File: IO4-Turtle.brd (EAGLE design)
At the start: 106.7 x 104.1 mm, 30 parts, among them CON2 RJ12/6, IC1 TC4428A, IC2 NE555S, Q1 PMBT2222, X1 0.156 Molex, X2 MSTBA5

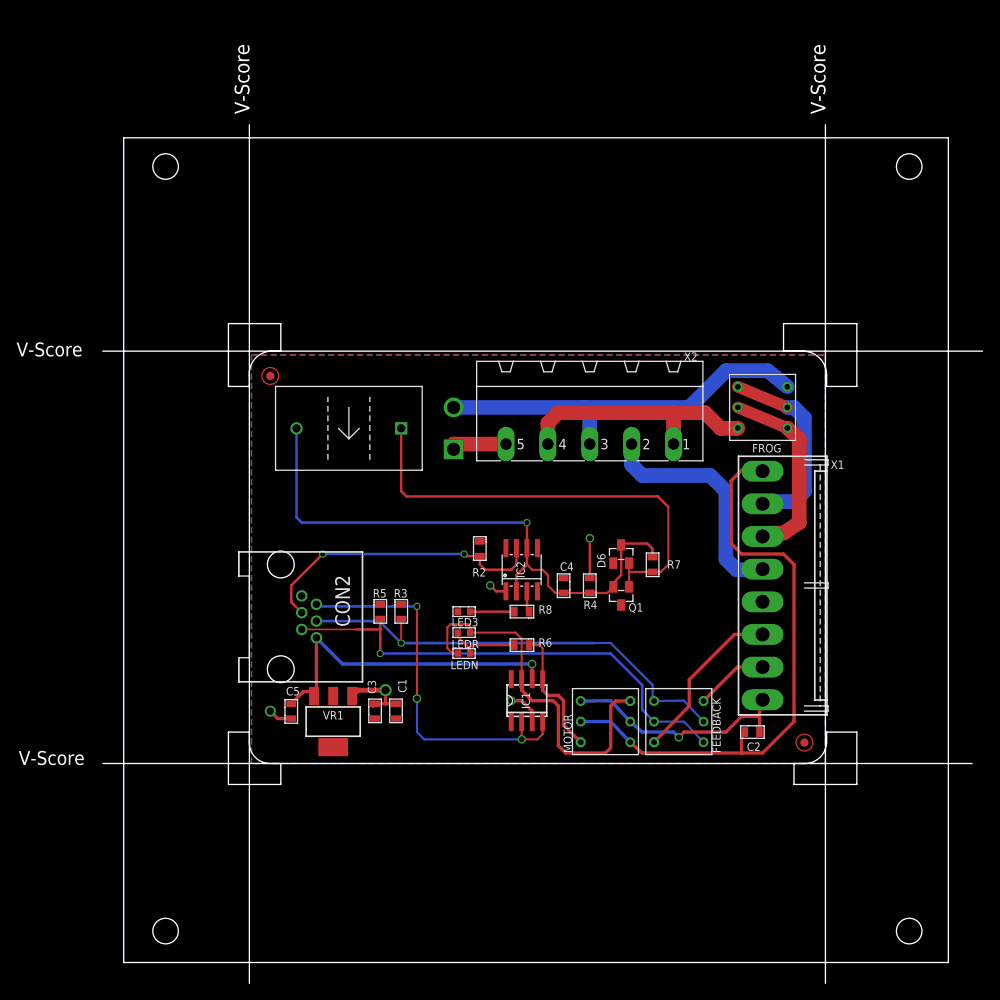
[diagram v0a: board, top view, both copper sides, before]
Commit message: cleanup, replaced LM1117 output cap
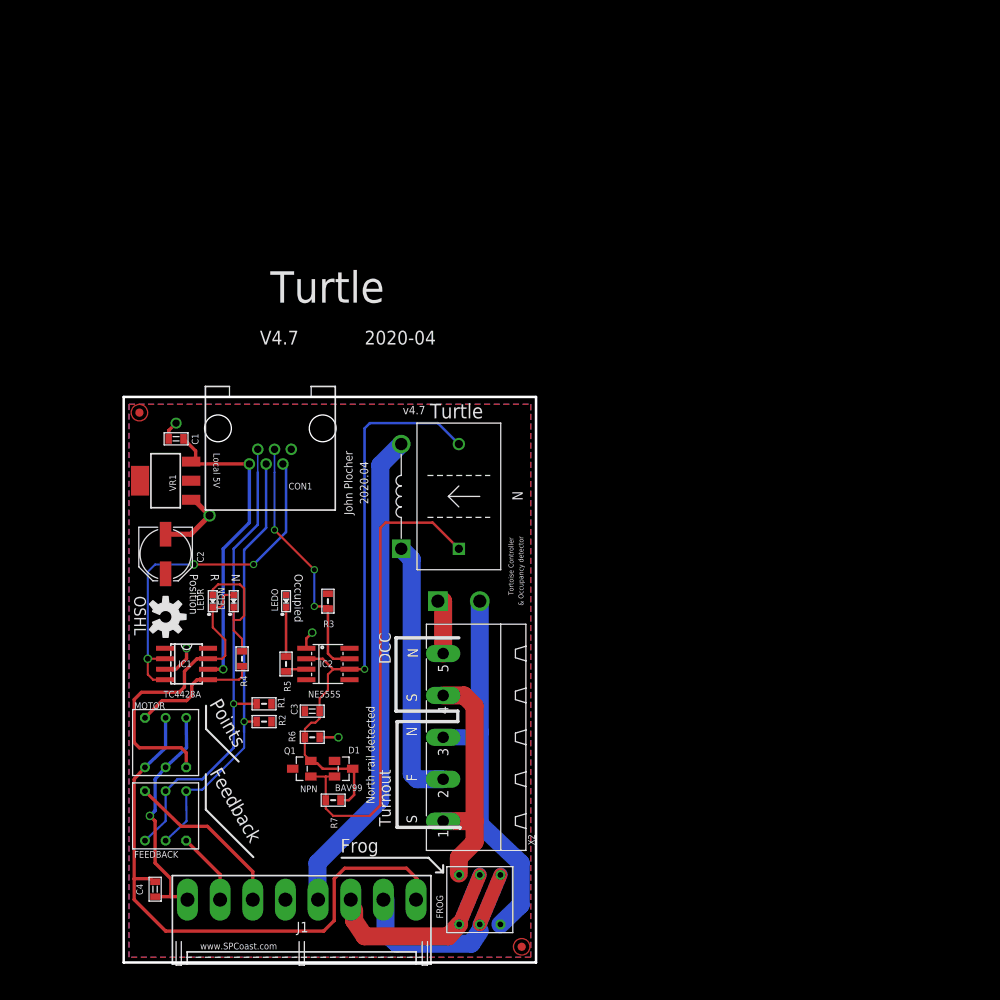
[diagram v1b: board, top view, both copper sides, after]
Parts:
- removed BOARD: BOARD70X50-HOHOLES, SPCoast:BOARD-7X5-TEMPLATE
- removed C5: 10uf, SPCoast:0805-CAP
- removed CON2: RJ12/6, SPCoast:RJ25-INVERTED
- removed D6: BAV99, SPCoast:SOT23
- removed LED3: Y, SPCoast:0603-LED
- removed R8: 1K0, SPCoast:0805-RES
- removed X1: 0.156 Molex, SPCoast:KK-156-8-F
- added CON1: RJ12/6, SPCoast:RJ25-INVERTED
- added D1: BAV99, SPCoast:SOT23
- added J1: (no value), SPCoast:KK-156-8-F
- added LEDO: Y, SPCoast:0603-LED
- added LMP1: (no value), SPCoast:BULB-3156
- added OSHW1: DOC-OSHW-LOGO-M, SPCoast:OSHW-LOGO-M
- added R1: 10k, SPCoast:0805-RES
- C2: value 0.1uf -> 100uf; device SPCoast:0805-CAP -> SPCoast:PANASONIC_D
- C3: value 10uf -> 2.2uf
- C4: value 2.2uf -> 0.1uf
- IC1: device tc442xa:SO-08 -> SPCoast:SO-08
- Q1: value PMBT2222 -> NPN
- R4: value 1M0 -> 2K0
- R5: value 10k -> 1K0
- R6: value 2K0 -> 1M0
- moved C2 74.3 mm to (5.08, 49.5), turned to 270 degrees
- moved FROG 68.8 mm to (43.2, 7.62), turned to 90 degrees
- moved FEEDBACK 63.3 mm to (5.08, 17.8), turned to 270 degrees
- moved C4 61.7 mm to (3.81, 8.89)
- moved MOTOR 53.4 mm to (5.08, 26.7), turned to 270 degrees
- moved R7 48.1 mm to (25.4, 19.7), turned to 180 degrees
- moved Q1 44.0 mm to (21.6, 23.5), turned to 90 degrees
- moved R4 43.1 mm to (14.4, 36.8)
- moved X2 42.6 mm to (43.8, 27.3), turned to 90 degrees
- moved C1 42.4 mm to (6.35, 63.5), turned to 180 degrees
- moved FID2 42.3 mm to (48.3, 1.91), turned to 270 degrees
- moved IC1 41.5 mm to (7.62, 36.2), turned to 270 degrees
- moved VR1 35.6 mm to (5.08, 58.4), turned to 90 degrees
- moved R2 33.5 mm to (17.0, 29.2), turned to 0 degrees
- moved LEDR 30.7 mm to (10.8, 43.8), turned to 270 degrees
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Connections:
- new net PROTECTED_FROG: J1.4, LMP1.P$2
- net !INORMAL: now also CON1.3, R2.1; no longer CON2.3, R3.1
- net !IOCCUPIED: now also CON1.4, R3.1; no longer CON2.4, R2.1
- net !IREVERSE: now also CON1.2, R1.1; no longer CON2.2, R5.1
- net !KNORMAL: now also CON1.5; no longer CON2.5
- net +12V: now also C1.1, CON1.1; no longer C5.1, CON2.1
- net FROG: now also LMP1.P$1; no longer X1.4
- net GND: now also C2.-, CON1.6, J1.5, R6.1; no longer C3.2, C5.2, CON2.6, R4.1, X1.5
- net M+: now also C4.1, J1.1; no longer C2.1, X1.1
- net M-: now also C4.2, J1.8; no longer C2.2, X1.8
- net N: now also J1.2; no longer X1.2
- net N$16: now also J1.6; no longer X1.6
- net N$17: now also J1.7; no longer X1.7
- net N$19: now also R4.2; no longer R6.2
- net N$2: now also D1.2; no longer D6.2
- net N$3: now also R4.1; no longer R6.1
- net N$8: now also LEDO.C, R5.1; no longer LED3.C, R8.1
- net N$9: now also R5.2; no longer R8.2
- net S: now also J1.3; no longer X1.3
- net TRIGGER: now also C3.2, D1.3, R6.2; no longer C4.2, D6.3, R4.2
- net V+: now also C2.+, LEDO.A, R1.2; no longer C1.1, C4.1, LED3.A, R5.2
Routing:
- net PROTECTED_FROG: track 0.00 -> 59.5 mm
- net N: track 23.9 -> 30.9 mm
- net N$1: track 45.4 -> 38.4 mm
- net N$3: track 8.77 -> 15.5 mm
- net S: track 23.5 -> 30.2 mm
- net !IOCCUPIED: track 36.3 -> 31.3 mm, vias 2 -> 3
- net FROG: track 28.6 -> 31.9 mm
- net N$2: track 55.8 -> 59.0 mm
- net !KNORMAL: track 46.9 -> 44.1 mm
- net GND: track 23.3 -> 20.4 mm
- net !INORMAL: track 56.0 -> 53.3 mm
- net TRIGGER: track 71.5 -> 73.3 mm
- net !IREVERSE: track 59.2 -> 57.7 mm
- net +12V: track 40.0 -> 38.7 mm
- net DCC-S: track 30.7 -> 29.4 mm
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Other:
- board size 106.7 x 104.1 mm -> 50 x 68.6 mm
- board text added: "2020-04"
- board text added: "2020.04"
- board text added: "C1"
- board text added: "C2"
- board text added: "C3"
- board text added: "C4"
- board text added: "CON1"
- board text added: "D1"
- board text added: "FEEDBACK"
- board text added: "FROG"
- board text added: "IC1"
- board text added: "IC2"
- board text added: "J1"
- board text added: "LEDN"
- board text added: "LEDO"
- board text added: "LEDR"
- board text added: "MOTOR"
- board text added: "NE555S"
- board text added: "OSHL"
- board text added: "Q1"
- board text added: "R1"
- board text added: "R2"
- board text added: "R3"
- board text added: "R4"
- board text added: "R5"
- board text added: "R6"
- board text added: "R7"
- board text added: "V4.7"
- board text added: "VR1"
- board text added: "X2"
- board text added: "v4.7"
- board text removed: "+"
- board text removed: "2018-03"
- board text removed: "2018.03"
- board text removed: "NE555"
- board text removed: "V4.6B"
- board text removed: "v4.6B"

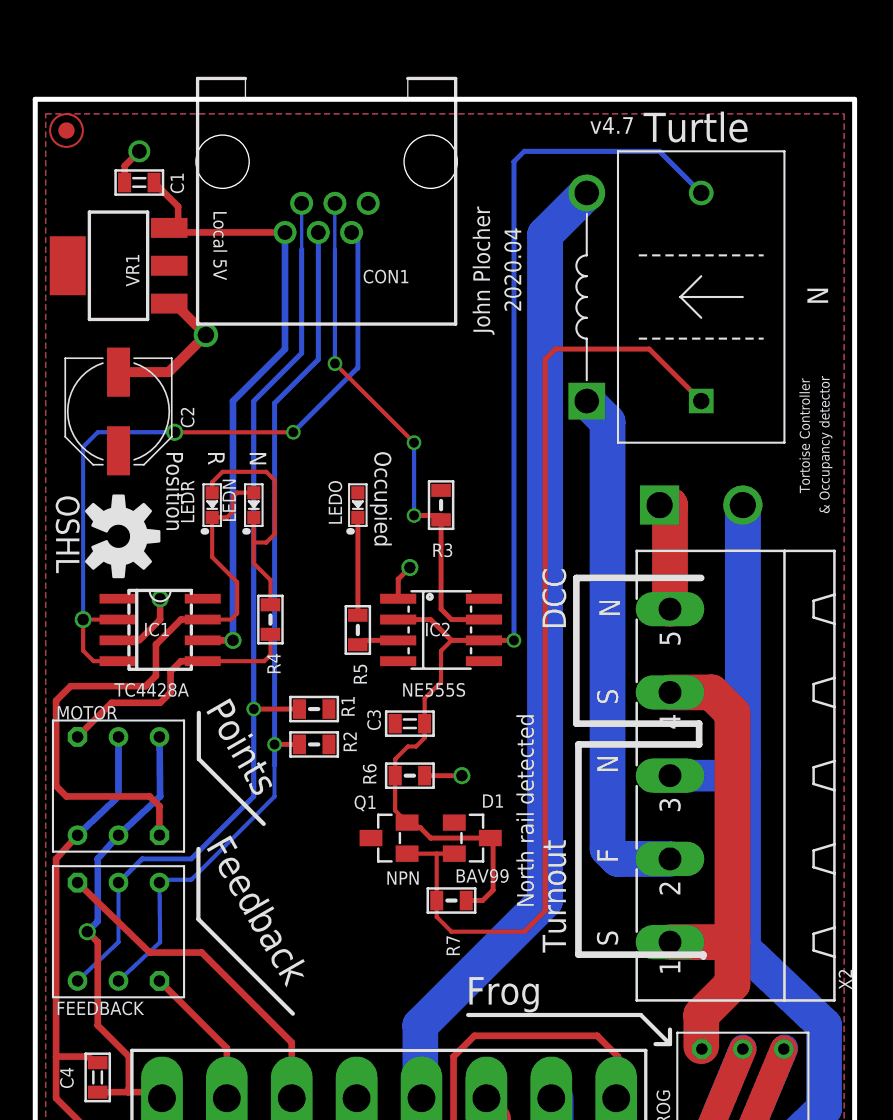
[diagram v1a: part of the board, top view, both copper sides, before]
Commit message: silkscreen cleanup, better power routing
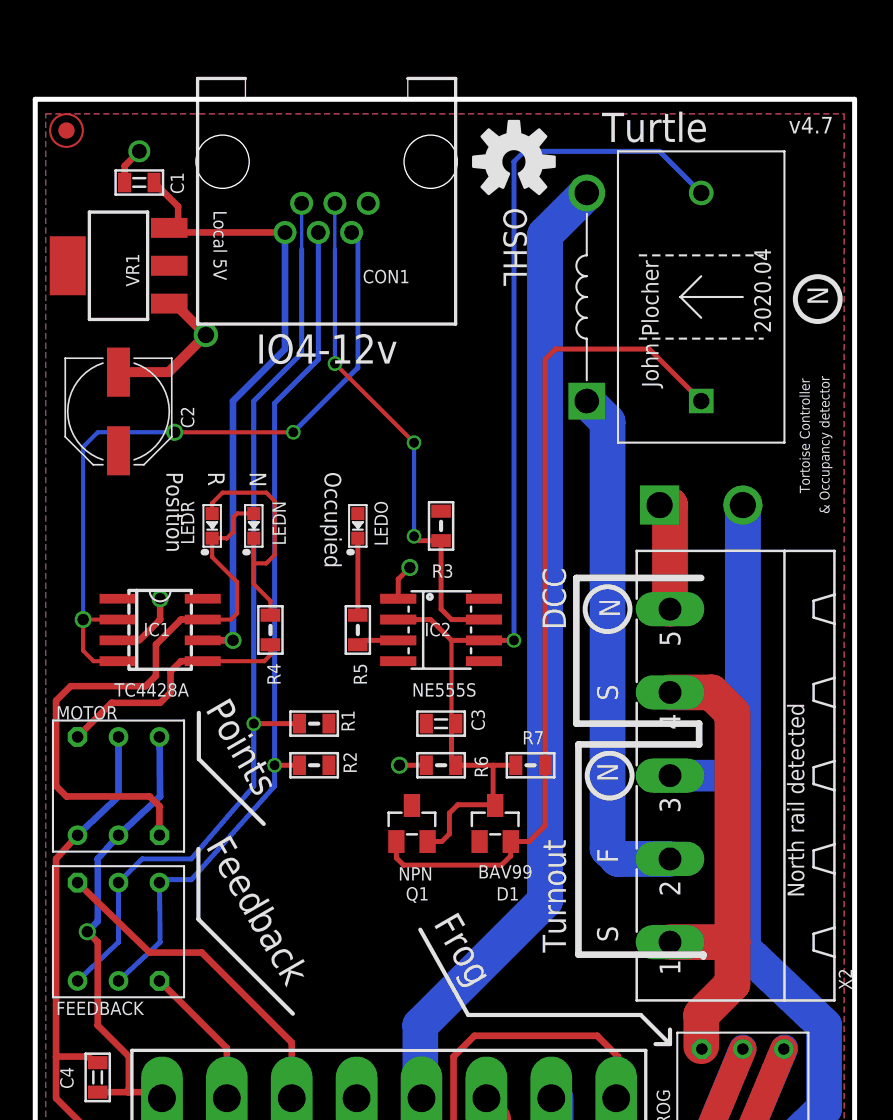
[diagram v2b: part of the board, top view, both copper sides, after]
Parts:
- moved OSHW1 33.2 mm to (29.2, 64.8), turned to 0 degrees
- moved R7 9.56 mm to (30.2, 27.9), turned to 0 degrees
- moved R6 2.01 mm to (24.8, 27.9), turned to 0 degrees
- moved C3 1.91 mm to (24.8, 30.5)
- moved D1 1.66 mm to (28.1, 24.4), turned to 0 degrees
- moved Q1 1.66 mm to (23.0, 24.4), turned to 0 degrees
- moved R2 1.27 mm to (17.0, 27.9)
- moved LEDN 1.27 mm to (13.3, 42.5)
- moved LEDO 1.27 mm to (19.7, 42.5)
- moved LEDR 1.27 mm to (10.8, 42.5)
- moved R3 1.27 mm to (24.8, 42.5)
- moved R1 0.89 mm to (17.0, 30.5)
- moved R4 0.63 mm to (14.4, 36.2)
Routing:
- net N$2: track 59.0 -> 51.3 mm
- net TRIGGER: track 73.3 -> 70.3 mm
- net N$8: track 5.97 -> 4.70 mm
- net N$1: track 38.4 -> 37.1 mm
- net N$3: track 15.5 -> 14.8 mm
- net GND: track 20.4 -> 19.8 mm
- net N$19: track 15.8 -> 15.2 mm
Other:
- board text added: "IO4-12v"
